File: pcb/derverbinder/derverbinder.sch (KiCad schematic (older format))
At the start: 10 parts, among them J1 Conn_01x16_Male

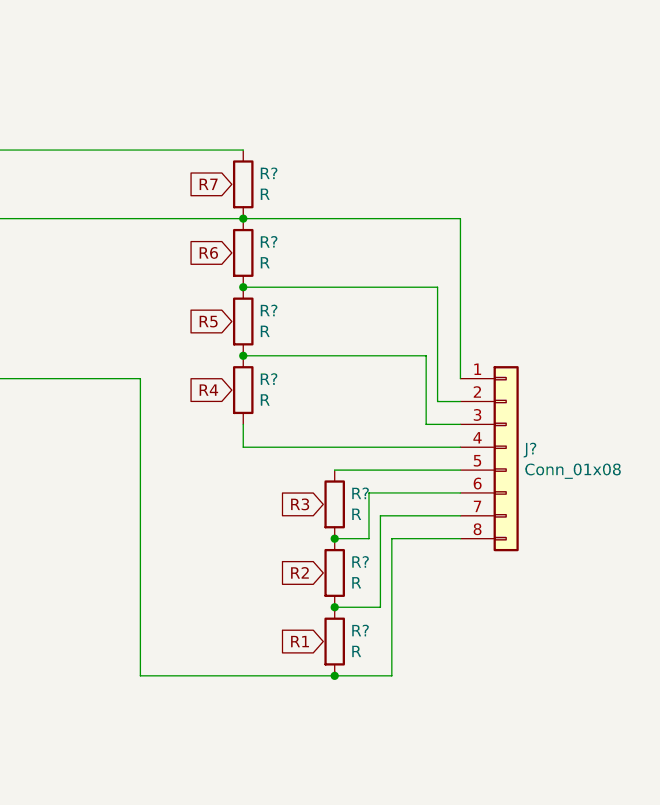
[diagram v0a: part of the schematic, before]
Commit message: PCB-Routing gemacht, PCB und Schema stimmen NICHT überein
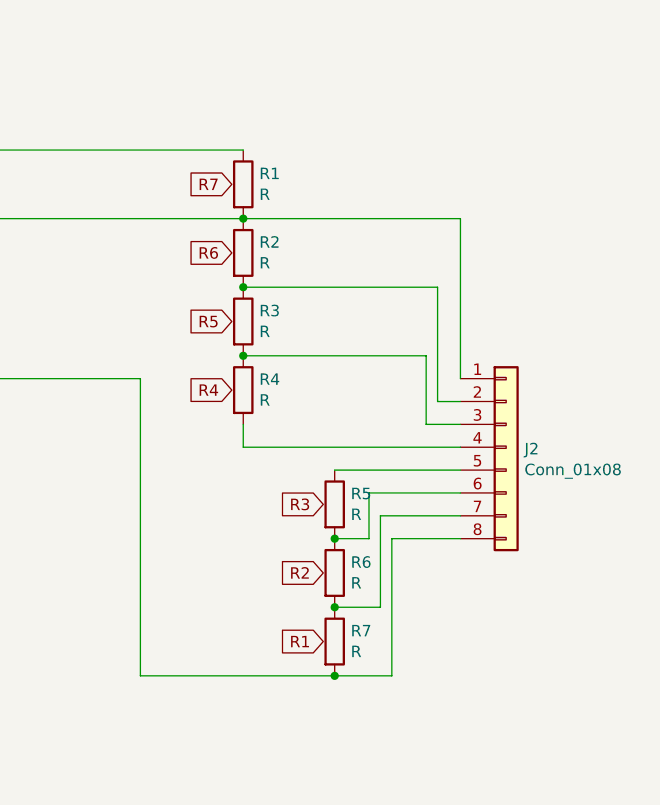
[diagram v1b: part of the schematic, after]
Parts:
- gave numbers to parts that had none: 8
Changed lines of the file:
@@
 EESchema Schematic File Version 4
+LIBS:derverbinder-cache
 EELAYER 30 0
 EELAYER END
@@
 	6350 4450 6550 4450
 $Comp
-L Device:R R?
+L Device:R R6
 U 1 1 5DB910AF
 P 9450 5300
-F 0 "R?" H 9520 5346 50  0000 L CNN
+F 0 "R6" H 9520 5346 50  0000 L CNN
 F 1 "R" H 9520 5255 50  0000 L CNN
 F 2 "" V 9380 5300 50  0001 C CNN
@@
 $EndComp
 $Comp
-L Connector_Generic:Conn_01x08 J?
+L Connector_Generic:Conn_01x08 J2
 U 1 1 5DB913E3
 P 10200 4750
-F 0 "J?" H 10280 4742 50  0000 L CNN
+F 0 "J2" H 10280 4742 50  0000 L CNN
 F 1 "Conn_01x08" H 10280 4651 50  0000 L CNN
 F 2 "" H 10200 4750 50  0001 C CNN
@@
 $EndComp
 $Comp
-L Device:R R?
+L Device:R R2
 U 1 1 5DB9716C
 P 9050 3900
-F 0 "R?" H 9120 3946 50  0000 L CNN
+F 0 "R2" H 9120 3946 50  0000 L CNN
 F 1 "R" H 9120 3855 50  0000 L CNN
 F 2 "" V 8980 3900 50  0001 C CNN
@@
 $EndComp
 $Comp
-L Device:R R?
+L Device:R R1
 U 1 1 5DB9777C
 P 9050 3600
-F 0 "R?" H 9120 3646 50  0000 L CNN
+F 0 "R1" H 9120 3646 50  0000 L CNN
 F 1 "R" H 9120 3555 50  0000 L CNN
 F 2 "" V 8980 3600 50  0001 C CNN
@@
 $EndComp
 $Comp
-L Device:R R?
+L Device:R R3
 U 1 1 5DB98608
 P 9050 4200
-F 0 "R?" H 9120 4246 50  0000 L CNN
+F 0 "R3" H 9120 4246 50  0000 L CNN
 F 1 "R" H 9120 4155 50  0000 L CNN
 F 2 "" V 8980 4200 50  0001 C CNN
@@
 $EndComp
 $Comp
-L Device:R R?
+L Device:R R7
 U 1 1 5DB98A26
 P 9450 5600
-F 0 "R?" H 9520 5646 50  0000 L CNN
+F 0 "R7" H 9520 5646 50  0000 L CNN
 F 1 "R" H 9520 5555 50  0000 L CNN
 F 2 "" V 9380 5600 50  0001 C CNN
@@
 $EndComp
 $Comp
-L Device:R R?
+L Device:R R5
 U 1 1 5DB99153
 P 9450 5000
-F 0 "R?" H 9520 5046 50  0000 L CNN
+F 0 "R5" H 9520 5046 50  0000 L CNN
 F 1 "R" H 9520 4955 50  0000 L CNN
 F 2 "" V 9380 5000 50  0001 C CNN
@@
 $EndComp
 $Comp
-L Device:R R?
+L Device:R R4
 U 1 1 5DB99B48
 P 9050 4500
-F 0 "R?" H 9120 4546 50  0000 L CNN
+F 0 "R4" H 9120 4546 50  0000 L CNN
 F 1 "R" H 9120 4455 50  0000 L CNN
 F 2 "" V 8980 4500 50  0001 C CNN
